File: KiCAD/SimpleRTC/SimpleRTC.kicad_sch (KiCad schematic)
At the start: 19 parts, among them J1 AVR-ISP-6, J2 Conn_01x04, J3 Conn_01x04, U1 ATtiny85-20P

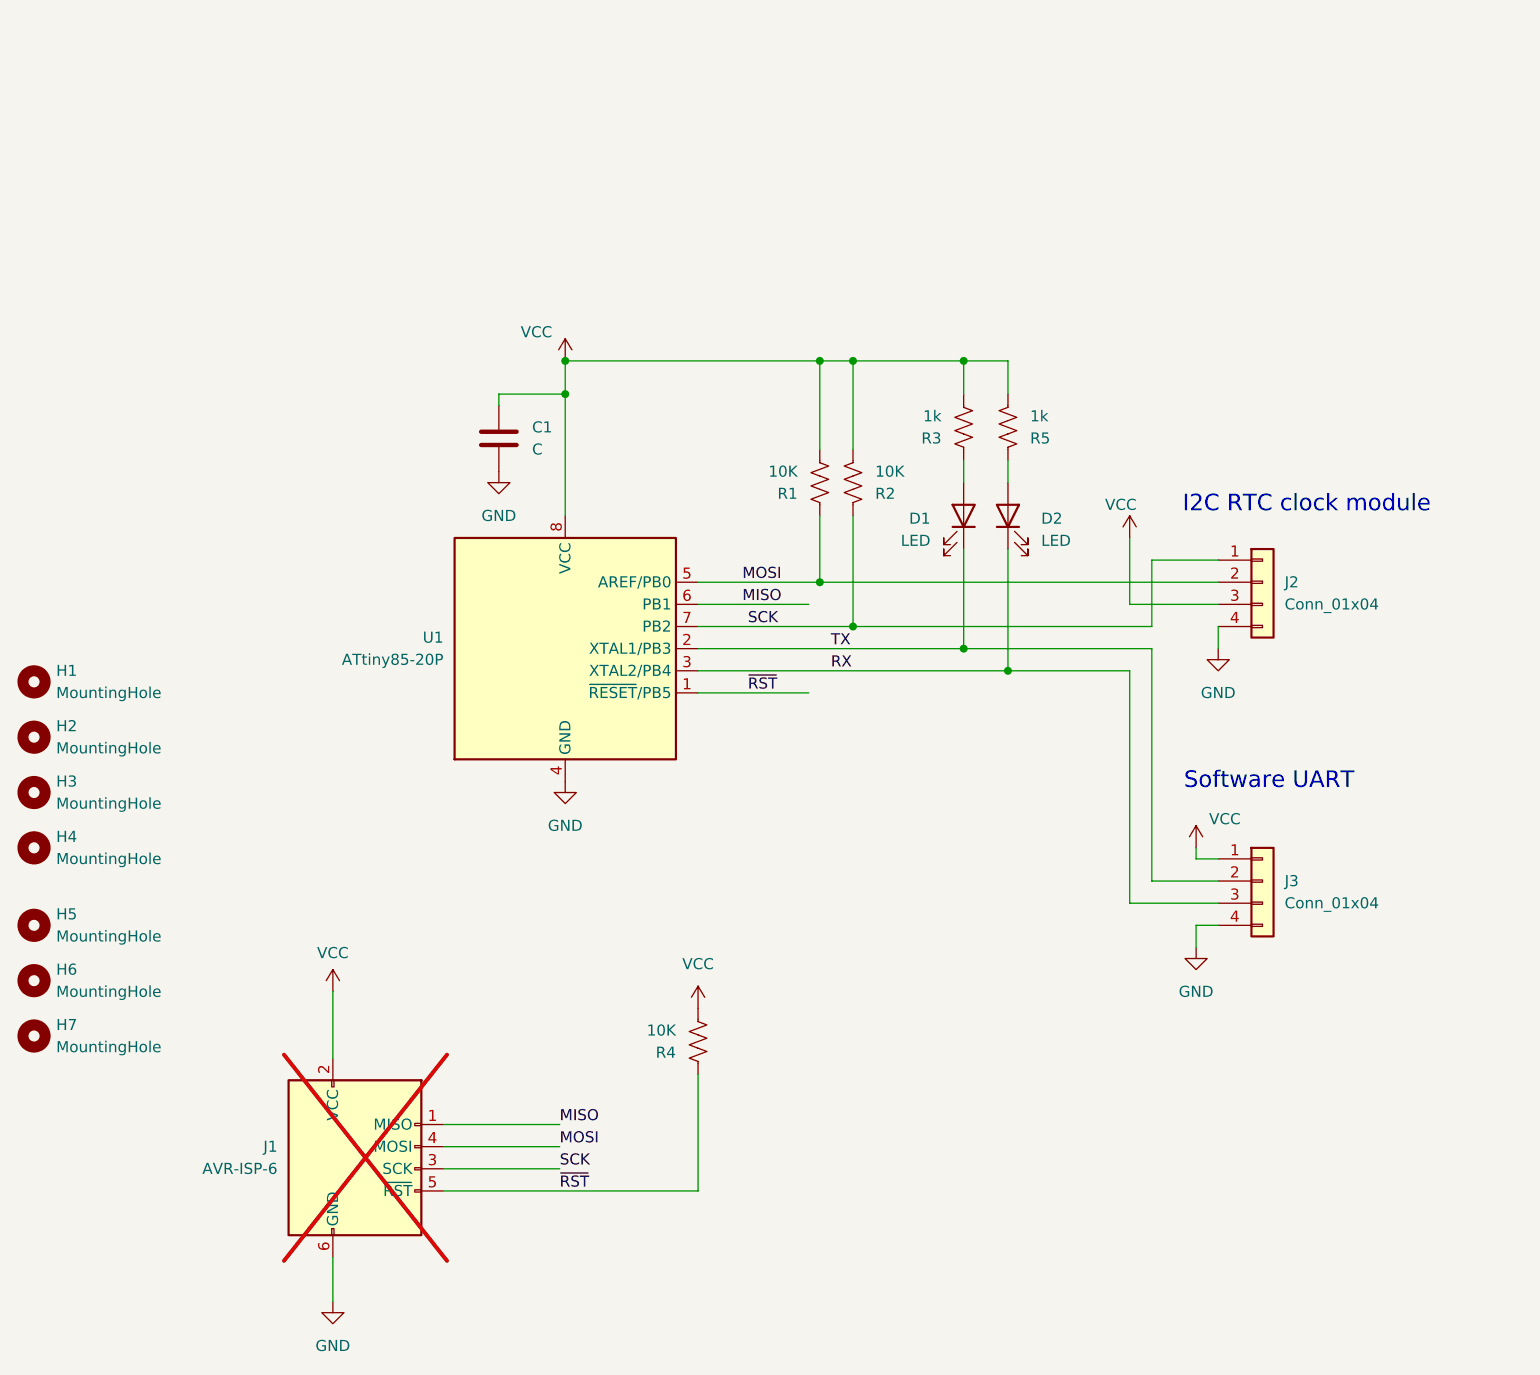
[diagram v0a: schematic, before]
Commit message: add buttons to simple RTC, change to ATTiny84
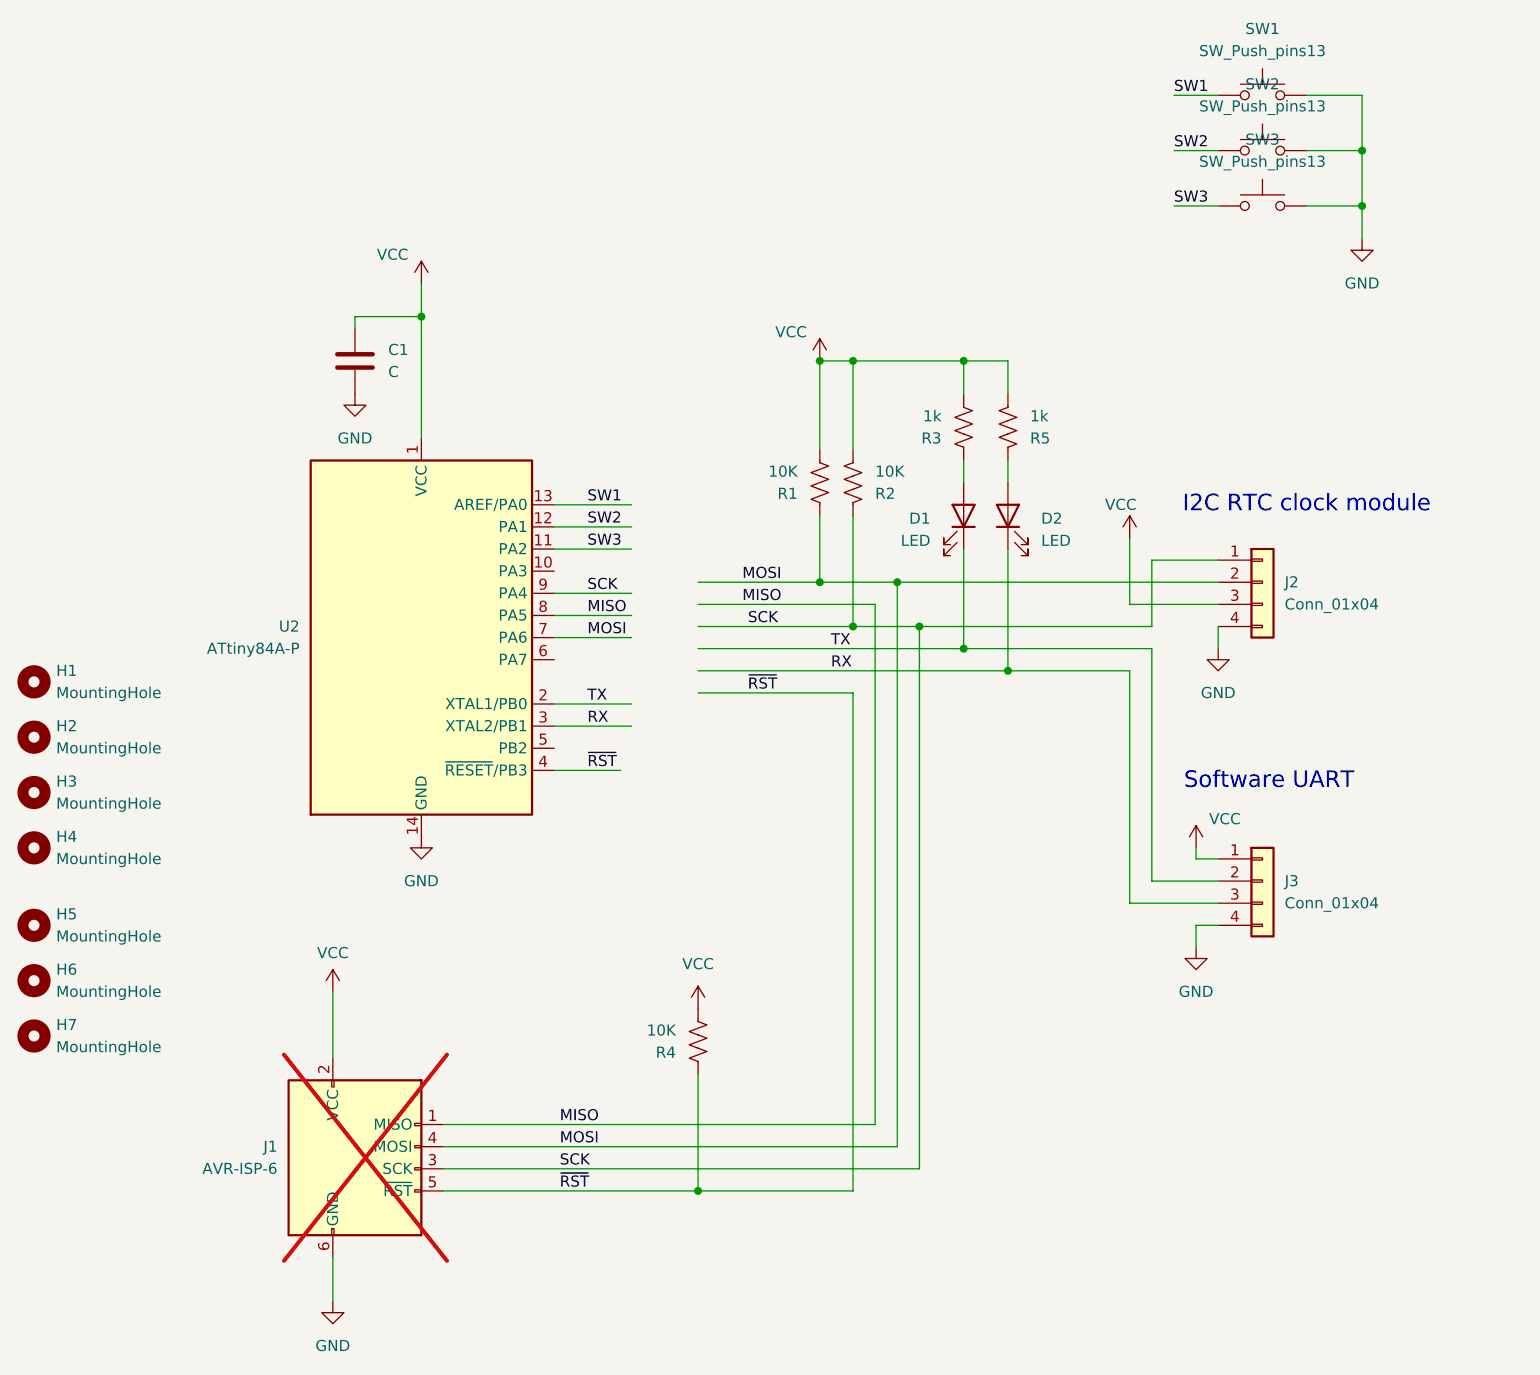
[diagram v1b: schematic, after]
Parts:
- removed U1: ATtiny85-20P, Package_DIP:DIP-8_W7.62mm, symbol MCU_Microchip_ATtiny:ATtiny85-20P
- added SW1, SW2, SW3: SW_Push_pins13, AA_parts:SW4_1825910-B_TEC, symbol my_sw:SW_Push_pins13
- added U2: ATtiny84A-P, Package_DIP:DIP-14_W7.62mm, symbol MCU_Microchip_ATtiny:ATtiny84A-P
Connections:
- net GND: now also SW1.3, SW2.3, SW3.3, U2.14 (GND)
- net MISO: now also U2.8 (PA5)
- net MOSI: now also U2.7 (PA6)
- net RX: now also U2.3 (XTAL2/PB1)
- net SCK: now also U2.9 (PA4)
- net TX: now also U2.2 (XTAL1/PB0)
- net VCC: now also U2.1 (VCC)
- net ~{RST}: now also U2.4 (~{RESET}/PB3)
- new net SW1: SW1.1, U2.13 (AREF/PA0)
- new net SW2: SW2.1, U2.12 (PA1)
- new net SW3: SW3.1, U2.11 (PA2)
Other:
- moved on the sheet: C1

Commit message: As built SimpleRTC design
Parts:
- J1: CatNo (none) -> A122759-ND; now fitted
- J2, J3: CatNo (none) -> 2057-PH1RB-04-UA-ND
- SW1, SW2, SW3: CatNo (none) -> 450-1157-ND
- U2: CatNo (none) -> ATTINY84A-PU-ND
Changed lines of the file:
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@@
 		(on_board yes)
 		(dnp no)
-		(fields_autoplaced yes)
 		(property "Reference" "J2"
 			(at 217.17 86.3599 0)
@@
 				)
 				(hide yes)
+			)
+		)
+		(property "CatNo" "2057-PH1RB-04-UA-ND"
+			(at 229.87 92.202 0)
+			(effects
+				(font
+					(size 1.27 1.27)
+				)
 			)
 		)
@@
 			)
 		)
+		(property "CatNo" "450-1157-ND"
+			(at 214.63 36.83 0)
+			(effects
+				(font
+					(size 1.27 1.27)
+				)
+				(hide yes)
+			)
+		)
 		(pin "3"
 		)
@@
 			)
 		)
+		(property "CatNo" "450-1157-ND"
+			(at 214.63 43.18 0)
+			(effects
+				(font
+					(size 1.27 1.27)
+				)
+				(hide yes)
+			)
+		)
 		(pin "3"
 		)
@@
 		(on_board yes)
 		(dnp no)
-		(fields_autoplaced yes)
 		(property "Reference" "J3"
 			(at 217.17 120.6499 0)
@@
 				)
 				(hide yes)
+			)
+		)
+		(property "CatNo" "2057-PH1RB-04-UA-ND"
+			(at 229.87 126.238 0)
+			(effects
+				(font
+					(size 1.27 1.27)
+				)
 			)
 		)
@@
 		(in_bom yes)
 		(on_board yes)
-		(dnp yes)
-		(fields_autoplaced yes)
+		(dnp no)
 		(property "Reference" "J1"
 			(at 101.6 151.1299 0)
@@
 				)
 				(hide yes)
+			)
+		)
+		(property "CatNo" "A122759-ND"
+			(at 93.726 156.972 0)
+			(effects
+				(font
+					(size 1.27 1.27)
+				)
 			)
 		)
@@
 		(on_board yes)
 		(dnp no)
-		(fields_autoplaced yes)
 		(property "Reference" "U2"
 			(at 104.14 91.4399 0)
@@
 			)
 		)
+		(property "CatNo" "ATTINY84A-PU-ND"
+			(at 95.758 96.266 0)
+			(effects
+				(font
+					(size 1.27 1.27)
+				)
+			)
+		)
 		(pin "2"
 		)
@@
 		(on_board yes)
 		(dnp no)
-		(fields_autoplaced yes)
 		(property "Reference" "SW1"
 			(at 214.63 22.86 0)
@@
 			)
 		)
+		(property "CatNo" "450-1157-ND"
+			(at 236.728 30.48 0)
+			(effects
+				(font
+					(size 1.27 1.27)
+				)
+			)
+		)

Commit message: modifying layout for V2
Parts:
- SW1, SW2, SW3: footprint AA_parts:SW4_1825910-B_TEC -> AA_parts:SW_1437565-3
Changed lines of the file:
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@@
 		)
 		(instances
-			(project ""
+			(project "SimpleRTC"
 				(path "/25dcc5eb-ed4b-4c36-b18e-fa7aa8c8b8de"
 					(reference "H1")
@@
 		)
 		(instances
-			(project ""
+			(project "SimpleRTC"
 				(path "/25dcc5eb-ed4b-4c36-b18e-fa7aa8c8b8de"
 					(reference "J2")
@@
 			)
 		)
-		(property "Footprint" "AA_parts:SW4_1825910-B_TEC"
+		(property "Footprint" "AA_parts:SW_1437565-3"
 			(at 214.63 31.75 0)
 			(effects
@@
 		)
 		(instances
-			(project ""
+			(project "SimpleRTC"
 				(path "/25dcc5eb-ed4b-4c36-b18e-fa7aa8c8b8de"
 					(reference "#PWR03")
@@
 			)
 		)
-		(property "Footprint" "AA_parts:SW4_1825910-B_TEC"
+		(property "Footprint" "AA_parts:SW_1437565-3"
 			(at 214.63 38.1 0)
 			(effects
@@
 		)
 		(instances
-			(project ""
+			(project "SimpleRTC"
 				(path "/25dcc5eb-ed4b-4c36-b18e-fa7aa8c8b8de"
 					(reference "J3")
@@
 		)
 		(instances
-			(project ""
+			(project "SimpleRTC"
 				(path "/25dcc5eb-ed4b-4c36-b18e-fa7aa8c8b8de"
 					(reference "D1")
@@
 		)
 		(instances
-			(project ""
+			(project "SimpleRTC"
 				(path "/25dcc5eb-ed4b-4c36-b18e-fa7aa8c8b8de"
 					(reference "U2")
@@
 			)
 		)
-		(property "Footprint" "AA_parts:SW4_1825910-B_TEC"
+		(property "Footprint" "AA_parts:SW_1437565-3"
 			(at 214.63 25.4 0)
 			(effects
@@
 		)
 		(instances
-			(project ""
+			(project "SimpleRTC"
 				(path "/25dcc5eb-ed4b-4c36-b18e-fa7aa8c8b8de"
 					(reference "SW1")
@@
 		)
 		(instances
-			(project ""
+			(project "SimpleRTC"
 				(path "/25dcc5eb-ed4b-4c36-b18e-fa7aa8c8b8de"
 					(reference "C1")
